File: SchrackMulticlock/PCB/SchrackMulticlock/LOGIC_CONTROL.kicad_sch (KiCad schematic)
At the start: 7 parts, among them U2 LDD080AUE-101A, U3 LTD080AUE-103A, U4 LDD080AUE-101A, U5 MAX7219

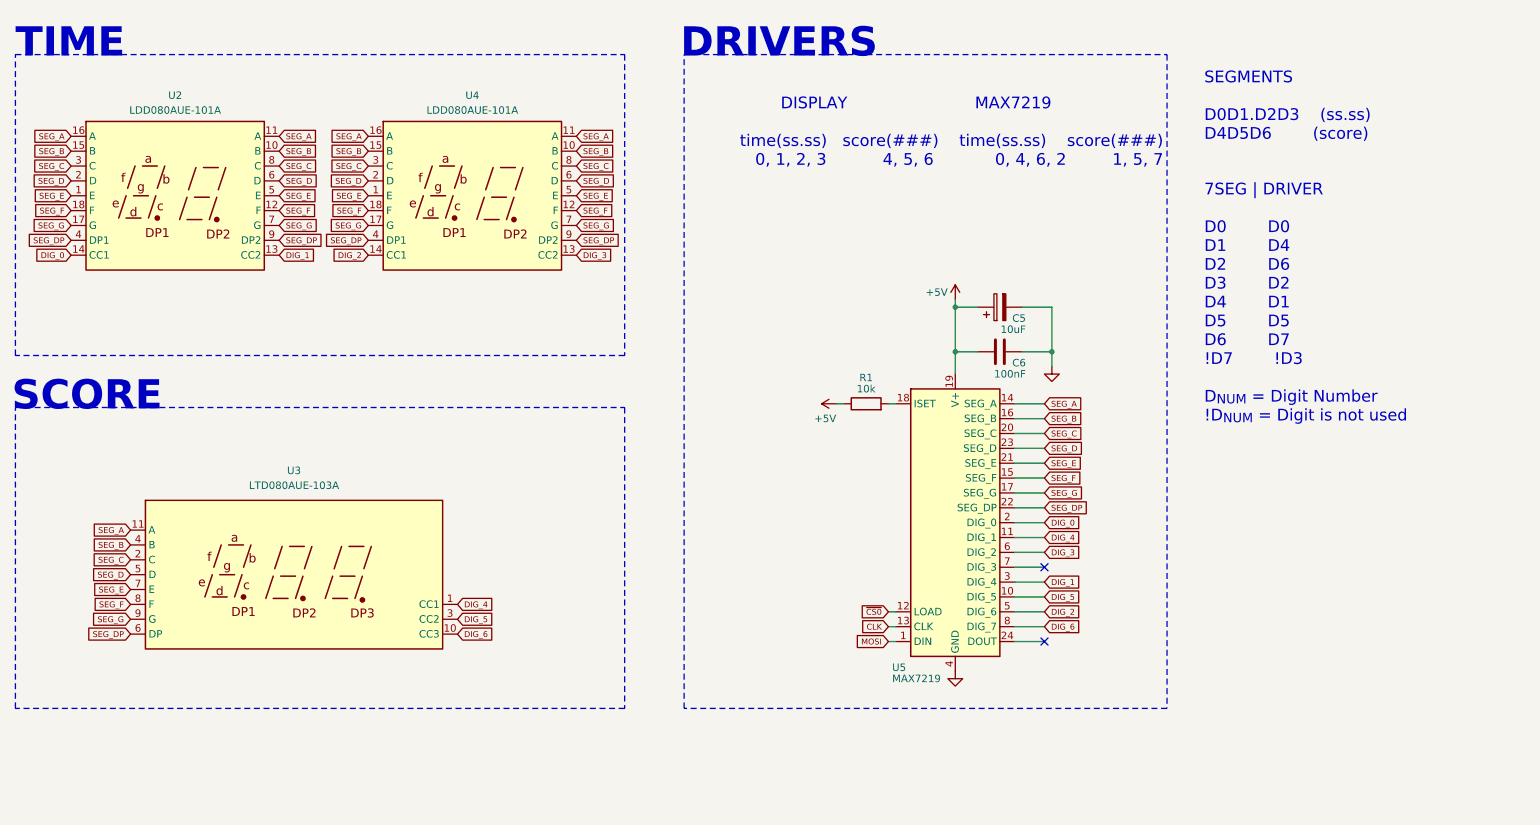
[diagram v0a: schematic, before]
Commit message: Stopwatch.h + Schematic update
Multiclock Scheamtic and code update
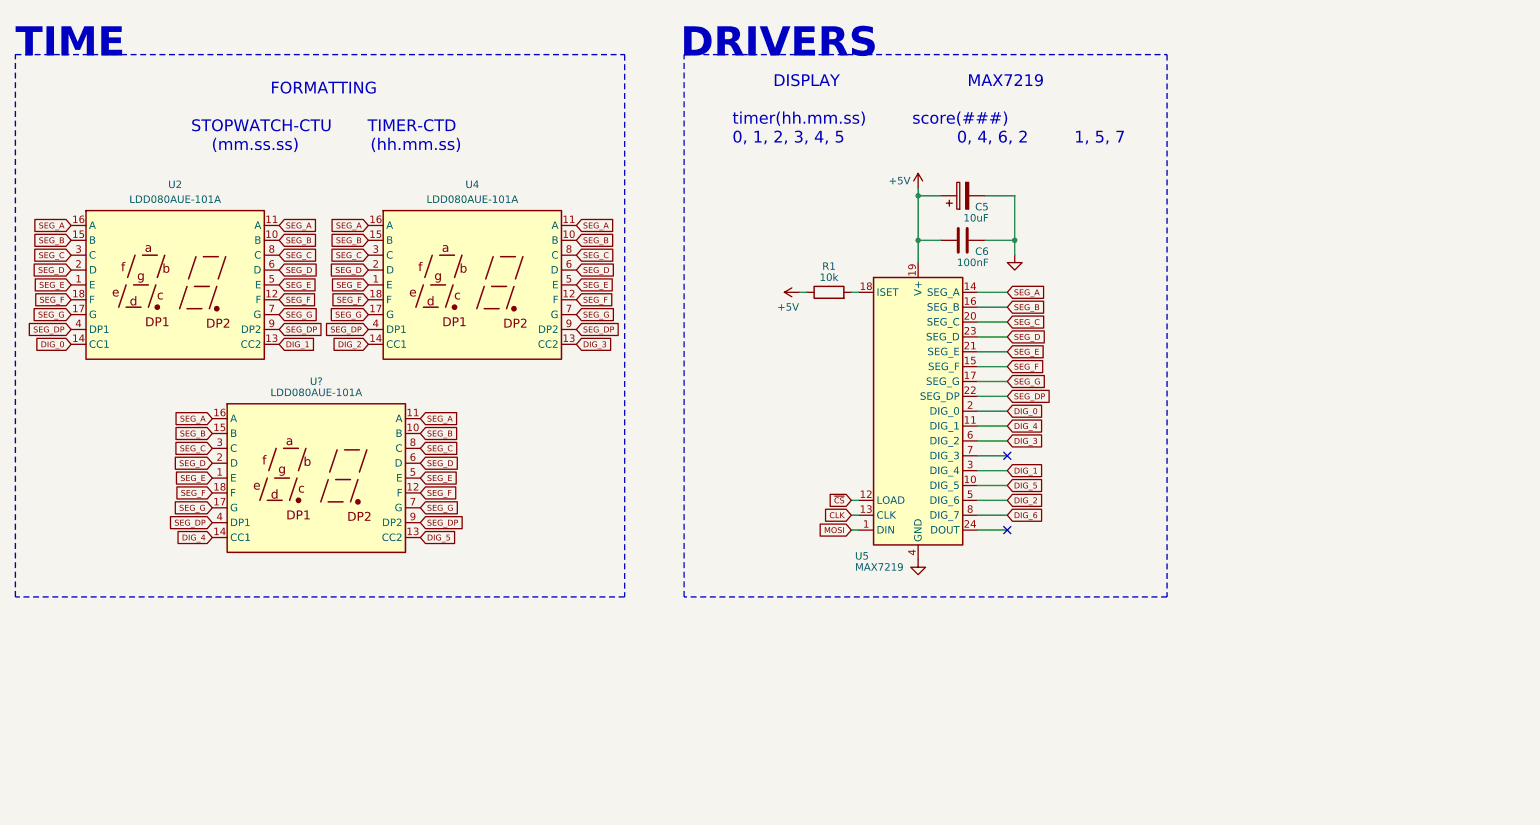
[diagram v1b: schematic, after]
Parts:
- removed U3: LTD080AUE-103A, Schrack_brd:WENRUN_LTD080x_7segment_3dig, symbol SchrackThingy_library:LTD080AUE-103A
- added U?: LDD080AUE-101A, Schrack_brd:WENRUN_LDD080x_7segment_2dig, symbol SchrackThingy_library:LDD080AUE-101A
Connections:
- net DIG_4: now also U?.14 (CC1)
- net DIG_5: now also U?.13 (CC2)
- net SEG_A: now also U?.11 (A), U?.16 (A)
- net SEG_B: now also U?.10 (B), U?.15 (B)
- net SEG_C: now also U?.3 (C), U?.8 (C)
- net SEG_D: now also U?.2 (D), U?.6 (D)
- net SEG_DP: now also U?.4 (DP1), U?.9 (DP2)
- net SEG_E: now also U?.1 (E), U?.5 (E)
- net SEG_F: now also U?.12 (F), U?.18 (F)
- net SEG_G: now also U?.17 (G), U?.7 (G)
- net ~{CS0} renamed ~{CS}
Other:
- note added: "DISPLAY MAX7219 timer(hh.mm.ss) score(###) 0, 1, 2, 3, 4, 5 0, 4, 6, 2 1, 5, 7"
- note added: "FORMATTING STOPWATCH-CTU TIMER-CTD (mm.ss.ss) (hh.mm.ss)"
- note removed: "7SEG | DRIVER D0 D0 D1 D4 D2 D6 D3 D2 D4 D1 D5 D5 D6 D7 !D7 !D3 D_{NUM} = Digit Number !D_{NUM} = Digit is not used"
- note removed: "DISPLAY MAX7219 time(ss.ss) score(###) time(ss.ss) score(###) 0, 1, 2, 3 4, 5, 6 0, 4, 6, 2 1, 5, 7"
- note removed: "SCORE"
- note removed: "SEGMENTS D0D1.D2D3 (ss.ss) D4D5D6 (score)"
- moved on the sheet: C5, C6, R1, U2, U4, U5

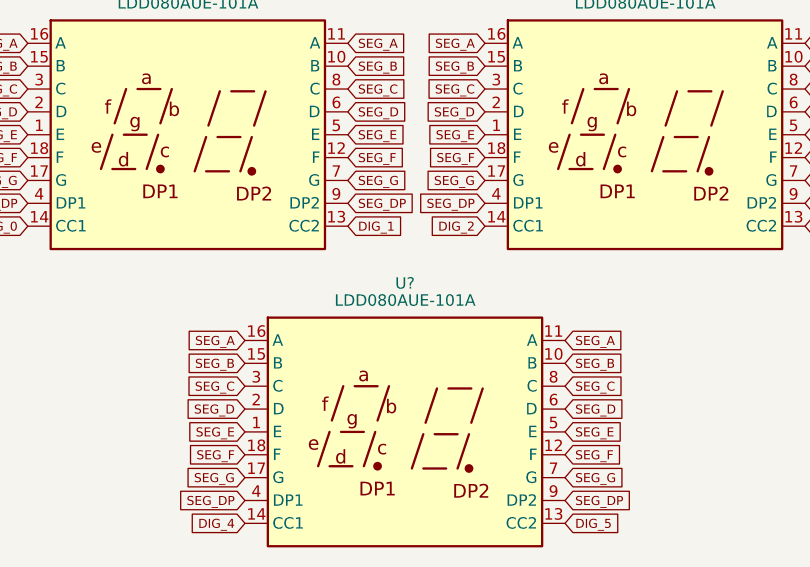
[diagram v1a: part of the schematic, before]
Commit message: SchrackMulticlock and Counter update
Schematic update for both
PCB update for Counter
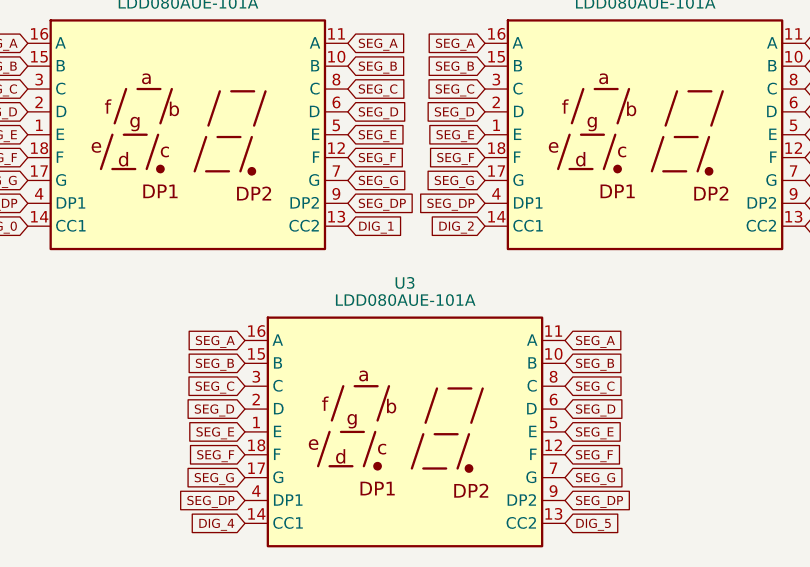
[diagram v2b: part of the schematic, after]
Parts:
- gave numbers to parts that had none: 1
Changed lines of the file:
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@@
 		(on_board yes)
 		(dnp no)
-		(property "Reference" "U?"
+		(property "Reference" "U3"
 			(at 97.79 90.17 0)
 			(effects
@@
 			(project "SchrackMulticlock"
 				(path "/d96f2ffc-3f4c-4f71-b693-29f6b8c3245d/50491303-1200-42ed-9e6c-90c20c198c18"
-					(reference "U?")
+					(reference "U3")
 					(unit 1)
 				)

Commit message: schrack multiclock schematic update
Just regular updates
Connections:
- net DIG_0: no longer U5.2 (DIG_0)
- net DIG_1: no longer U5.3 (DIG_4)
- net DIG_2: no longer U5.5 (DIG_6)
- net DIG_3: no longer U5.6 (DIG_2)
- net DIG_4: no longer U5.11 (DIG_1)
- net DIG_5: no longer U5.10 (DIG_5)
- net DIG_6: no longer U5.8 (DIG_7)
- no-connect marks 2 -> 1

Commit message: SchrackMulticlock schematic
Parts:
- added U9: LDD080AUE-101A, Display_7Segment:DA04-11SURKWA, symbol SchrackThingy_library:LDD080AUE-101A
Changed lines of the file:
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@@
-		)
-	)
-	(global_label "DIG_6"
-		(shape input)
-		(at 219.71 113.03 0)
-		(fields_autoplaced yes)
-		(effects
-			(font
-				(face "Bahnschrift")
-				(size 1 1)
-				(color 0 0 0 1)
-			)
-			(justify left)
-		)
-		(property "Intersheetrefs" "${INTERSHEET_REFS}"
-			(at 225.4072 113.03 0)
-			(effects
-				(font
-					(size 1.27 1.27)
-				)
-				(justify left)
-				(hide yes)
-			)
 		)
 	)
@@
 		(dnp no)
 		(fields_autoplaced yes)
-		(property "Reference" "#PWR09"
+		(property "Reference" "#PWR0106"
 			(at 217.17 74.93 0)
 			(effects
@@
 			(project "SchrackCounter"
 				(path "/d96f2ffc-3f4c-4f71-b693-29f6b8c3245d/50491303-1200-42ed-9e6c-90c20c198c18"
-					(reference "#PWR09")
+					(reference "#PWR0106")
 					(unit 1)
 				)
@@
 		(on_board yes)
 		(dnp no)
-		(property "Reference" "#PWR07"
+		(property "Reference" "#PWR0107"
 			(at 200.66 60.96 0)
 			(effects
@@
 			(project "SchrackCounter"
 				(path "/d96f2ffc-3f4c-4f71-b693-29f6b8c3245d/50491303-1200-42ed-9e6c-90c20c198c18"
-					(reference "#PWR07")
+					(reference "#PWR0107")
 					(unit 1)
 				)
@@
 	)
 	(symbol
+		(lib_id "SchrackThingy_library:LDD080AUE-101A")
+		(at 74.93 151.13 0)
+		(unit 1)
+		(exclude_from_sim no)
+		(in_bom yes)
+		(on_board yes)
+		(dnp no)
+		(property "Reference" "U9"
+			(at 74.93 133.985 0)
+			(effects
+				(font
+					(size 1.27 1.27)
+				)
+			)
+		)
+		(property "Value" "LDD080AUE-101A"
+			(at 74.93 136.525 0)
+			(effects
+				(font
+					(size 1.27 1.27)
+				)
+			)
+		)
+		(property "Footprint" "Display_7Segment:DA04-11SURKWA"
+			(at 74.422 134.112 0)
+			(effects
+				(font
+					(size 1.27 1.27)
+				)
+				(hide yes)
+			)
+		)
+		(property "Datasheet" ""
+			(at 72.644 129.54 0)
+			(effects
+				(font
+					(size 1.27 1.27)
+				)
+				(hide yes)
+			)
+		)
+		(property "Description" "2 digit 7 segment red LED, common cathode symbol custom made by bismarx"
+			(at 73.66 132.08 0)
+			(effects
+				(font
+					(size 1.27 1.27)
+				)
+				(hide yes)
+			)
+		)
+		(property "Product" "https://www.tme.eu/cz/en/details/ldd080aue-101a/7-segment-led-displays/wenrun/ldd080aue-101a-01/"
+			(at 81.534 129.794 0)
+			(effects
+				(font
+					(size 1.27 1.27)
+				)
+				(hide yes)
+			)
+		)
+		(property "Made by" "bismarx"
+			(at 74.93 151.13 0)
+			(effects
+				(font
+					(size 1.27 1.27)
+				)
+				(hide yes)
+			)
+		)
+		(pin "12"
+		)
+		(pin "10"
+		)
+		(pin "2"
+		)
+		(pin "3"
+		)
+		(pin "9"
+		)
+		(pin "6"
+		)
+		(pin "4"
+		)
+		(pin "18"
+		)
+		(pin "1"
+		)
+		(pin "5"
+		)
+		(pin "14"
+		)
+		(pin "16"
+		)
+		(pin "15"
+		)
+		(pin "11"
+		)
+		(pin "17"
+		)
+		(pin "13"
+		)
+		(pin "7"
+		)
+		(pin "8"
+		)
+		(instances
+			(project "SchrackMulticlock"
+				(path "/d96f2ffc-3f4c-4f71-b693-29f6b8c3245d/50491303-1200-42ed-9e6c-90c20c198c18"
+					(reference "U9")
+					(unit 1)
+				)
+			)
+		)
+	)
+	(symbol
 		(lib_id "power:+5V")
 		(at 180.34 74.93 90)
@@
 		(on_board yes)
 		(dnp no)
-		(property "Reference" "#PWR06"
+		(property "Reference" "#PWR0109"
 			(at 184.15 74.93 0)
 			(effects
@@
 			(project "SchrackCounter"
 				(path "/d96f2ffc-3f4c-4f71-b693-29f6b8c3245d/50491303-1200-42ed-9e6c-90c20c198c18"
-					(reference "#PWR06")
+					(reference "#PWR0109")
 					(unit 1)
 				)
@@
 		(dnp no)
 		(fields_autoplaced yes)
-		(property "Reference" "#PWR08"
+		(property "Reference" "#PWR0108"
 			(at 200.66 127 0)
 			(effects
@@
 			(project "SchrackCounter"
 				(path "/d96f2ffc-3f4c-4f71-b693-29f6b8c3245d/50491303-1200-42ed-9e6c-90c20c198c18"
-					(reference "#PWR08")
+					(reference "#PWR0108")
 					(unit 1)
 				)

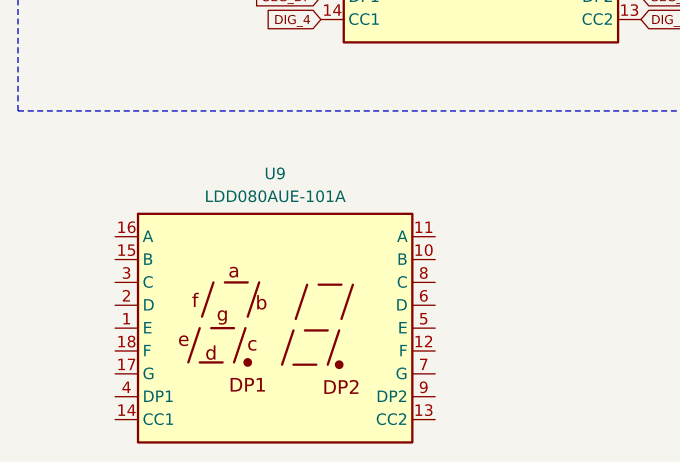
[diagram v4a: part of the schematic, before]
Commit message: Schrackcounter Prototype update
Schematic + PCB update, final version
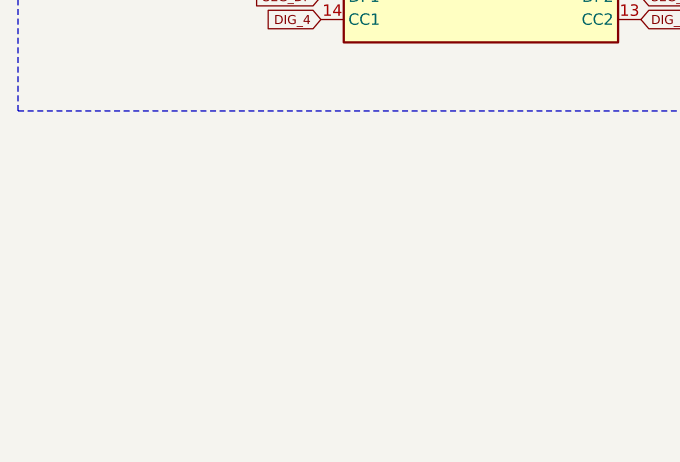
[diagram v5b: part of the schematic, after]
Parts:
- removed U9: LDD080AUE-101A, Display_7Segment:DA04-11SURKWA, symbol SchrackThingy_library:LDD080AUE-101A
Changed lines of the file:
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@@
-	)
-	(symbol
-		(lib_id "SchrackThingy_library:LDD080AUE-101A")
-		(at 74.93 151.13 0)
-		(unit 1)
-		(exclude_from_sim no)
-		(in_bom yes)
-		(on_board yes)
-		(dnp no)
-		(property "Reference" "U9"
-			(at 74.93 133.985 0)
-			(effects
-				(font
-					(size 1.27 1.27)
-				)
-			)
-		)
-		(property "Value" "LDD080AUE-101A"
-			(at 74.93 136.525 0)
-			(effects
-				(font
-					(size 1.27 1.27)
-				)
-			)
-		)
-		(property "Footprint" "Display_7Segment:DA04-11SURKWA"
-			(at 74.422 134.112 0)
-			(effects
-				(font
-					(size 1.27 1.27)
-				)
-				(hide yes)
-			)
-		)
-		(property "Datasheet" ""
-			(at 72.644 129.54 0)
-			(effects
-				(font
-					(size 1.27 1.27)
-				)
-				(hide yes)
-			)
-		)
-		(property "Description" "2 digit 7 segment red LED, common cathode symbol custom made by bismarx"
-			(at 73.66 132.08 0)
-			(effects
-				(font
-					(size 1.27 1.27)
-				)
-				(hide yes)
-			)
-		)
-		(property "Product" "https://www.tme.eu/cz/en/details/ldd080aue-101a/7-segment-led-displays/wenrun/ldd080aue-101a-01/"
-			(at 81.534 129.794 0)
-			(effects
-				(font
-					(size 1.27 1.27)
-				)
-				(hide yes)
-			)
-		)
-		(property "Made by" "bismarx"
-			(at 74.93 151.13 0)
-			(effects
-				(font
-					(size 1.27 1.27)
-				)
-				(hide yes)
-			)
-		)
-		(pin "12"
-		)
-		(pin "10"
-		)
-		(pin "2"
-		)
-		(pin "3"
-		)
-		(pin "9"
-		)
-		(pin "6"
-		)
-		(pin "4"
-		)
-		(pin "18"
-		)
-		(pin "1"
-		)
-		(pin "5"
-		)
-		(pin "14"
-		)
-		(pin "16"
-		)
-		(pin "15"
-		)
-		(pin "11"
-		)
-		(pin "17"
-		)
-		(pin "13"
-		)
-		(pin "7"
-		)
-		(pin "8"
-		)
-		(instances
-			(project "SchrackMulticlock"
-				(path "/d96f2ffc-3f4c-4f71-b693-29f6b8c3245d/50491303-1200-42ed-9e6c-90c20c198c18"
-					(reference "U9")
-					(unit 1)
-				)
-			)
-		)
 	)
 	(symbol

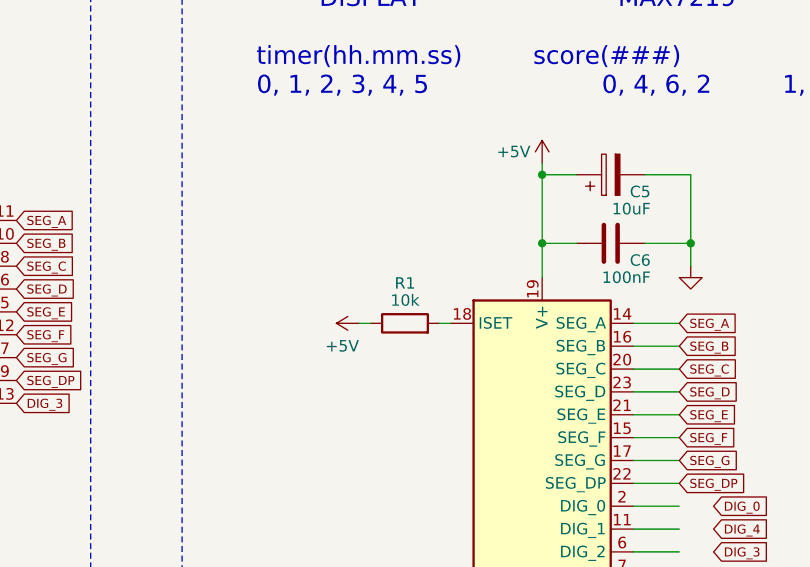
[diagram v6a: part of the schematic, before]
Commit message: SchrackMulticlock and Counter pcb updates
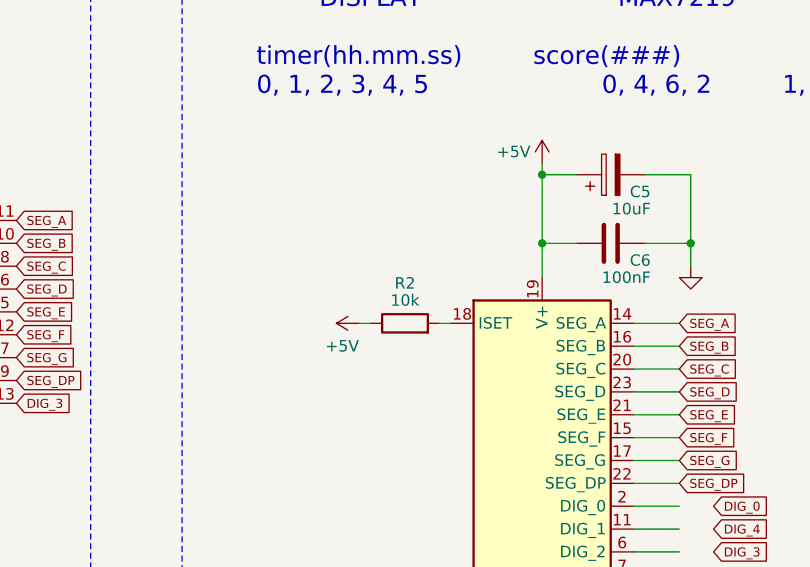
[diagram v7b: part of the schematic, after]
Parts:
- renumbered R1 to R2
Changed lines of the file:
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@@
 		(dnp no)
 		(fields_autoplaced yes)
-		(property "Reference" "#PWR09"
+		(property "Reference" "#PWR011"
 			(at 217.17 74.93 0)
 			(effects
@@
 			(project "SchrackCounter"
 				(path "/d96f2ffc-3f4c-4f71-b693-29f6b8c3245d/50491303-1200-42ed-9e6c-90c20c198c18"
-					(reference "#PWR09")
+					(reference "#PWR011")
 					(unit 1)
 				)
@@
 		(on_board yes)
 		(dnp no)
-		(property "Reference" "#PWR07"
+		(property "Reference" "#PWR09"
 			(at 200.66 60.96 0)
 			(effects
@@
 			(project "SchrackCounter"
 				(path "/d96f2ffc-3f4c-4f71-b693-29f6b8c3245d/50491303-1200-42ed-9e6c-90c20c198c18"
-					(reference "#PWR07")
+					(reference "#PWR09")
 					(unit 1)
 				)
@@
 		(on_board yes)
 		(dnp no)
-		(property "Reference" "R1"
+		(property "Reference" "R2"
 			(at 185.42 70.485 90)
 			(effects
@@
 			(project "SchrackCounter"
 				(path "/d96f2ffc-3f4c-4f71-b693-29f6b8c3245d/50491303-1200-42ed-9e6c-90c20c198c18"
-					(reference "R1")
+					(reference "R2")
 					(unit 1)
 				)
@@
 		(on_board yes)
 		(dnp no)
-		(property "Reference" "#PWR06"
+		(property "Reference" "#PWR08"
 			(at 184.15 74.93 0)
 			(effects
@@
 			(project "SchrackCounter"
 				(path "/d96f2ffc-3f4c-4f71-b693-29f6b8c3245d/50491303-1200-42ed-9e6c-90c20c198c18"
-					(reference "#PWR06")
+					(reference "#PWR08")
 					(unit 1)
 				)
@@
 		(dnp no)
 		(fields_autoplaced yes)
-		(property "Reference" "#PWR08"
+		(property "Reference" "#PWR010"
 			(at 200.66 127 0)
 			(effects
@@
 			(project "SchrackCounter"
 				(path "/d96f2ffc-3f4c-4f71-b693-29f6b8c3245d/50491303-1200-42ed-9e6c-90c20c198c18"
-					(reference "#PWR08")
-					(unit 1)
-				)
+					(reference "#PWR010")
+					(unit 1)
+				)
